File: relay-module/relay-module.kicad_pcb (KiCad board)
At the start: 2 copper layers, 80 x 22 mm, 21 parts, among them K1 SRD-05VDC-SL-C, Q1 S8050, Q2 PC817X2NSZ9F, Q3 PC817X2NSZ9F

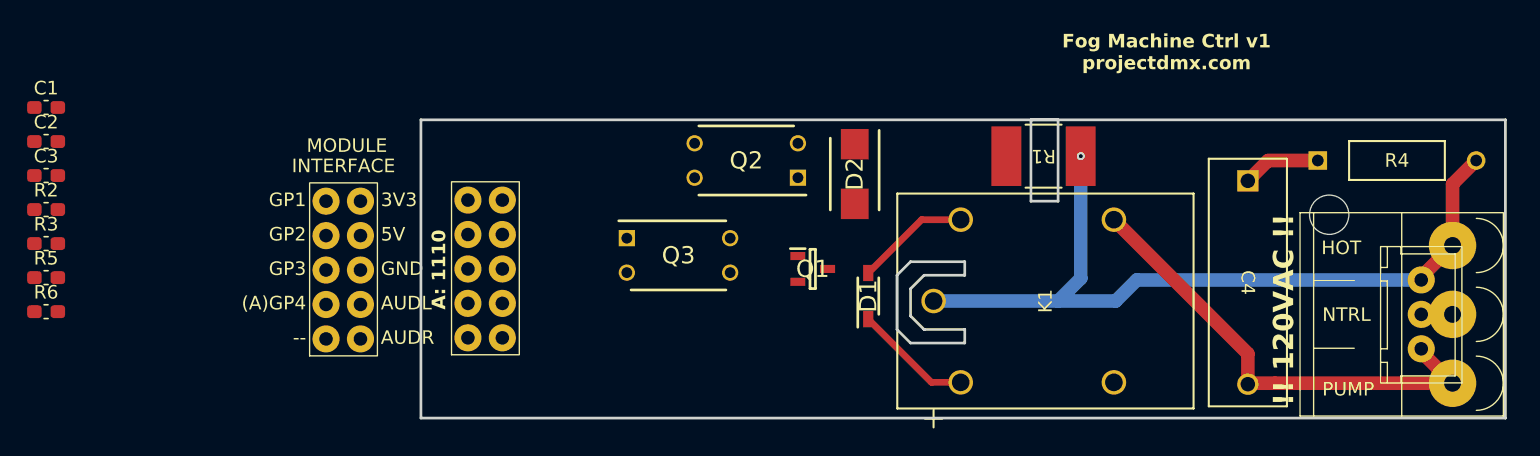
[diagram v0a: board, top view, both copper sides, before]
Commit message: finish relay + start rfid
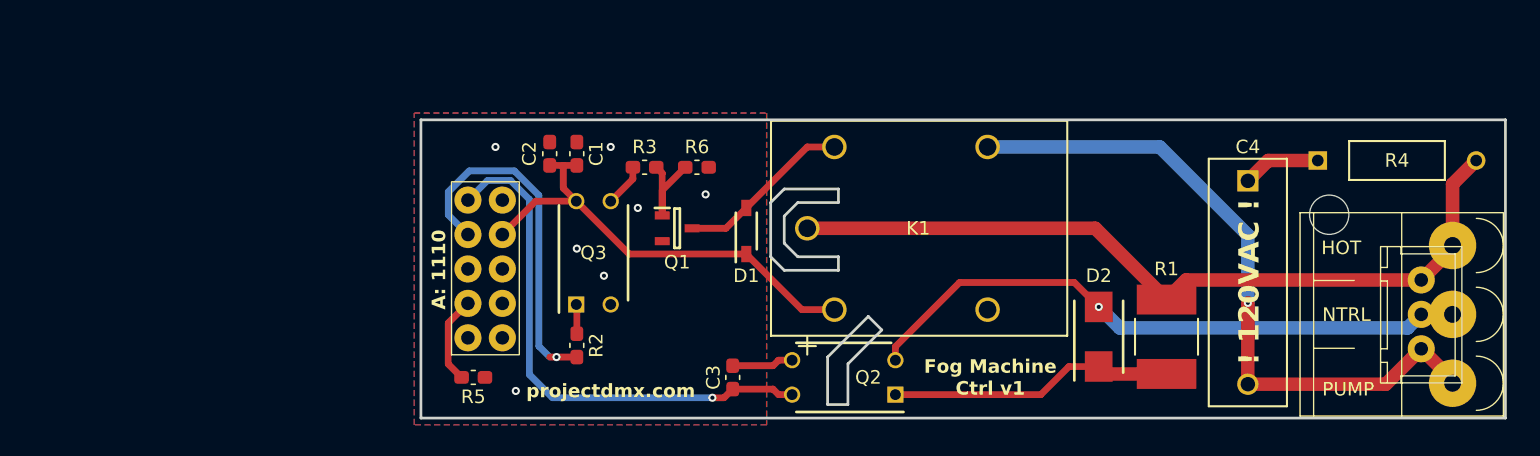
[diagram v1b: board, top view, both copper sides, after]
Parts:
- removed U1: ~, ProjectDMX:Module Interface
- moved C3 52.8 mm to (127.0, 111.0), turned to 90 degrees
- moved R6 49.2 mm to (124.4, 95.5), turned to 180 degrees
- moved R3 44.5 mm to (120.5, 95.5), turned to 180 degrees
- moved R2 40.4 mm to (115.5, 108.6), turned to -90 degrees
- moved C1 39.3 mm to (115.5, 94.5), turned to -90 degrees
- moved C2 37.2 mm to (113.5, 94.5), turned to -90 degrees
- moved R5 32.4 mm to (107.9, 111.0), turned to 180 degrees
- moved D2 21.6 mm to (154.0, 108.0), turned to 90 degrees
- moved Q2 17.5 mm to (135.2, 111.0)
- moved R1 16.1 mm to (159.0, 108.0), turned to -90 degrees
- moved K1 10.8 mm to (149.0, 100.0)
- moved Q1 10.4 mm to (122.9, 100.0)
- moved D1 10.2 mm to (128.0, 100.2)
- moved Q3 6.27 mm to (116.7, 101.8), turned to 90 degrees
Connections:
- REF** pad 7: Net-(U1-GP3) -> unconnected-(U1-GP3-Pad3)
- REF** pad 9: Net-(U1-GP1) -> Net-(Q2-COLLECTOR)
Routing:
- net Net-(Q2-CATHODE): track 2.31 -> 43.6 mm, vias 0 -> 1
- net Net-(Q2-COLLECTOR): track 0.00 -> 39.2 mm, vias 0 -> 1
- net Net-(U1-GP2): track 0.00 -> 26.1 mm, vias 0 -> 1
- net 5V: track 8.75 -> 33.9 mm
- net Net-(Q2-ANODE): track 0.00 -> 21.1 mm
- net Net-(K1-NO): track 34.9 -> 50.3 mm, vias 0 -> 1
- net Net-(Q1-B): track 0.00 -> 7.99 mm
- net Net-(U1-AGP4): track 0.00 -> 6.47 mm
- net GND: track 0.00 -> 4.55 mm, vias 0 -> 7
- net Net-(K1-C2): track 8.45 -> 13.0 mm
- net Net-(Q3-EMITTER): track 0.00 -> 3.18 mm
- net Net-(Q3-ANODE): track 0.00 -> 2.17 mm
- net Net-(K1-COM): track 58.5 -> 58.6 mm, vias 1 -> 0
- added copper zone on B.Cu, net GND
- added copper zone on F.Cu, net GND
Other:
- outline, holes or cut-outs redrawn
- board text added: "! 120VAC !"
- board text added: "Fog Machine Ctrl v1"
- board text added: "projectdmx.com"
- board text removed: "!! 120VAC !!"
- board text removed: "Fog Machine Ctrl v1 projectdmx.com"

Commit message: finish everything
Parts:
- removed R5: 10kΩ, Capacitor_SMD:C_0603_1608Metric_Pad1.08x0.95mm_HandSolder
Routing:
- net Net-(U1-AGP4): track 6.47 -> 0.00 mm
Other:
- board text removed: "A: 1110"

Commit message: small changes
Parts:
- Q1: value S8050 -> SOT95P240X115-3N
- Q2, Q3: value PC817X2NSZ9F -> DIP762W60P254L460H450Q4N
- moved R4 1.12 mm to (170.7, 94.0)
- moved D2 0.82 mm to (154.8, 108.0)
- moved C4 0.50 mm to (165.5, 96.5)
- moved R1 0.50 mm to (159.5, 108.0)
- moved Q2 0.26 mm to (135.1, 111.2)
- moved K1 0.18 mm to (149.0, 100.2)
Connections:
- REF** pad 1: (no net) -> Net-(Q2-COLLECTOR)
- REF** pad 2: (no net) -> Net-(U1-GP2)
- REF** pad 3: GND -> unconnected-(U1-GP3-Pad3)
- REF** pad 4: 5V -> Net-(U1-AGP4)
- REF** pad 6: Net-(U1-AGP4) -> 5V
- REF** pad 7: unconnected-(U1-GP3-Pad3) -> GND
- REF** pad 8: Net-(U1-GP2) -> (no net)
- REF** pad 9: Net-(Q2-COLLECTOR) -> (no net)
- U4 pad 1: Net-(K1-COM) -> Net-(K1-NO)
- U4 pad 3: Net-(K1-NO) -> Net-(K1-COM)
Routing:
- net Net-(K1-COM): track 58.6 -> 60.0 mm
- net Net-(K1-NO): track 50.3 -> 49.1 mm
- net Net-(Q2-ANODE): track 21.1 -> 21.8 mm
- net Net-(C4-Pad1): track 5.78 -> 6.49 mm
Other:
- outline, holes or cut-outs redrawn
- board text added: "120VAC"
- board text removed: "! 120VAC !"
